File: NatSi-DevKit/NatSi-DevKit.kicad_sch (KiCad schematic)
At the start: 47 parts, among them J1 USB_TypeC, J2 Conn_01x22_Pin, J3 Conn_01x22_Pin, J4 MEM2067-02-180-00-A_REVB, SW1 SW_Push, SW2 SW_Push, SW3 SW_Push, U1 USBLC6-2SC6, U2 ESP32-S3-WROOM-1, U3 NCP1117-3.3_SOT223

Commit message: PCB update - traces
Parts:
- J1: footprint sumec_brd:USB_Type_C -> sumec_brd:HRO_TYPE-C-31-M-12
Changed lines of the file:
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@@
 			)
 		)
-		(property "Footprint" "sumec_brd:USB_Type_C"
+		(property "Footprint" "sumec_brd:HRO_TYPE-C-31-M-12"
 			(at 133.35 167.64 0)
 			(effects

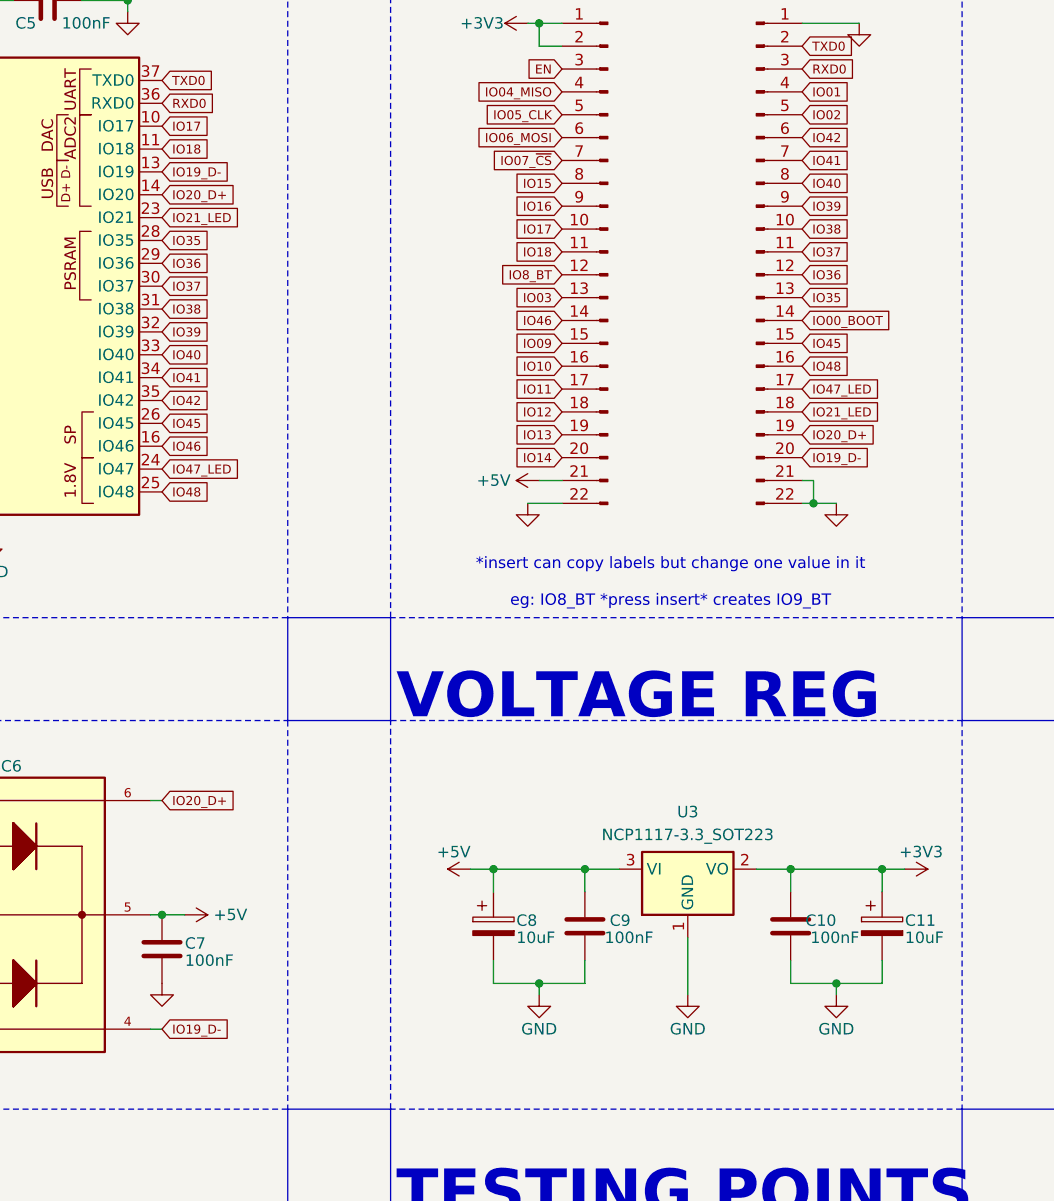
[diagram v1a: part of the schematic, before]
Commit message: Board update silkscreen and rouitign
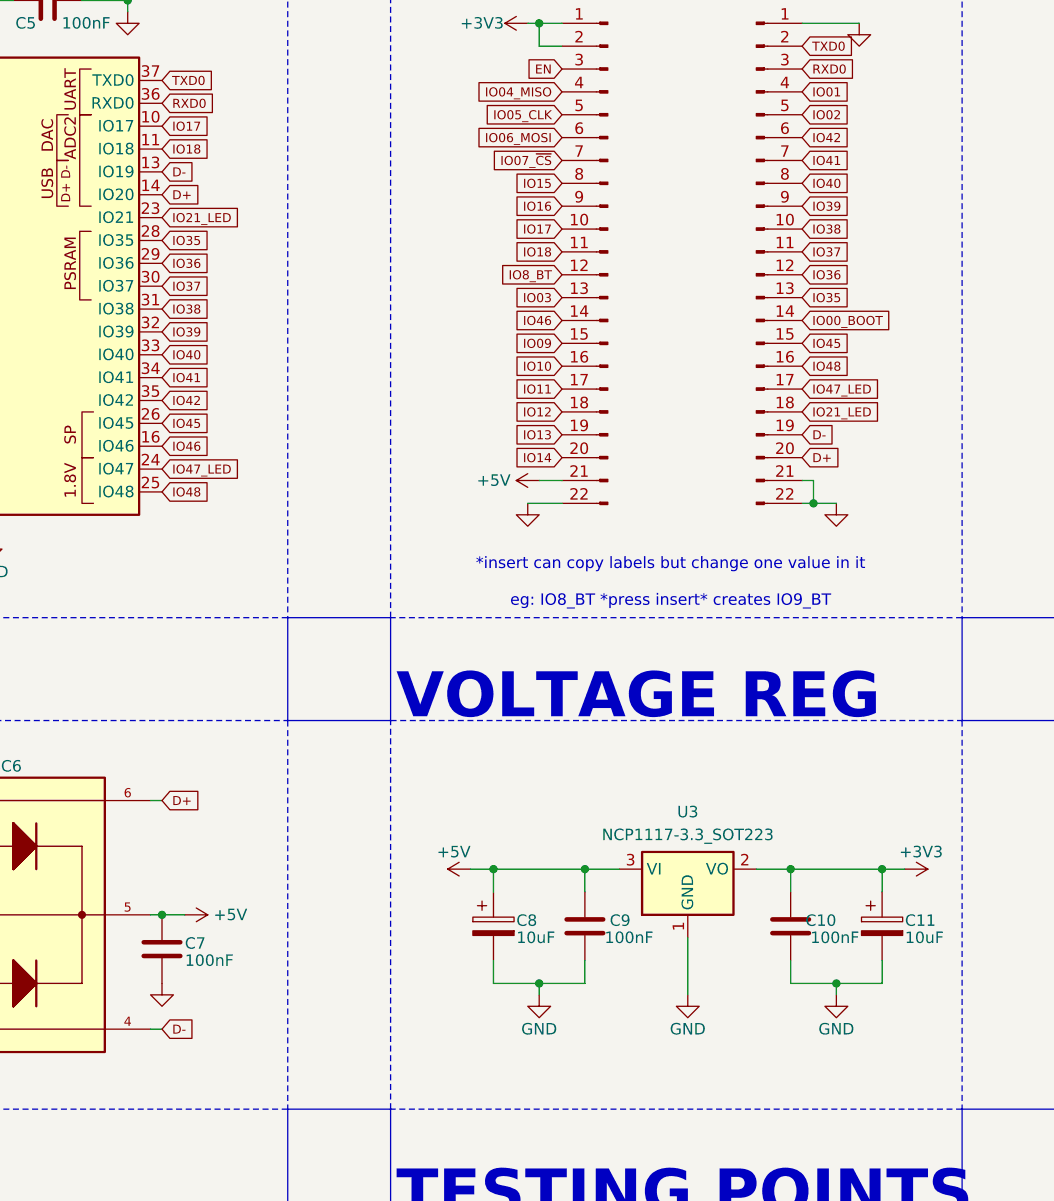
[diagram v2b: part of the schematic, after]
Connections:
- net IO19_D- renamed D-
- net D-: now also J3.19 (Pin_19); no longer J3.20 (Pin_20)
- net IO20_D+ renamed D+
- net D+: now also J3.20 (Pin_20); no longer J3.19 (Pin_19)

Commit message: Booard update
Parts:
- removed TP3: TestPoint, TestPoint:TestPoint_THTPad_D1.5mm_Drill0.7mm, symbol Connector:TestPoint
- SW1, SW2: footprint sumec_brd:SW_SPST_EVQPE1 -> Button_Switch_SMD:SW_SPST_B3U-1000P
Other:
- moved on the sheet: TP1, TP2
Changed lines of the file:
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@@
 	(wire
 		(pts
-			(xy 256.54 226.06) (xy 256.54 222.25)
+			(xy 265.43 224.79) (xy 265.43 220.98)
 		)
 		(stroke
@@
 	(wire
 		(pts
-			(xy 243.84 226.06) (xy 243.84 222.25)
+			(xy 252.73 224.79) (xy 252.73 220.98)
 		)
 		(stroke
@@
 	(wire
 		(pts
-			(xy 269.24 226.06) (xy 269.24 222.25)
-		)
-		(stroke
-			(width 0)
-			(type default)
-		)
-	)
-	(wire
-		(pts
 			(xy 247.65 67.31) (xy 247.65 69.85)
 		)
@@
 	(text "BOOT"
 		(exclude_from_sim no)
-		(at 143.51 214.63 0)
+		(at 146.05 213.995 0)
 		(effects
 			(font
@@
 				(color 0 0 0 1)
 			)
-			(justify left bottom)
 		)
 	)
@@
 	(text "ENABLE\nRESET"
 		(exclude_from_sim no)
-		(at 120.015 214.63 0)
+		(at 123.19 212.725 0)
 		(effects
 			(font
@@
 				(color 0 0 0 1)
 			)
-			(justify left bottom)
 		)
 	)
@@
 	(symbol
 		(lib_id "Connector:TestPoint")
-		(at 256.54 222.25 0)
+		(at 265.43 220.98 0)
 		(unit 1)
 		(exclude_from_sim no)
@@
 		(dnp no)
 		(property "Reference" "TP2"
-			(at 258.318 217.678 0)
+			(at 267.208 216.408 0)
 			(effects
 				(font
@@
 		)
 		(property "Value" "TestPoint"
-			(at 258.318 220.218 0)
+			(at 267.208 218.948 0)
 			(effects
 				(font
@@
 		)
 		(property "Footprint" "TestPoint:TestPoint_THTPad_D1.5mm_Drill0.7mm"
-			(at 261.62 222.25 0)
+			(at 270.51 220.98 0)
 			(effects
 				(font
@@
 		)
 		(property "Datasheet" "~"
-			(at 261.62 222.25 0)
+			(at 270.51 220.98 0)
 			(effects
 				(font
@@
 		)
 		(property "Description" "test point"
-			(at 256.54 222.25 0)
+			(at 265.43 220.98 0)
 			(effects
 				(font
@@
 	(symbol
 		(lib_id "power:+5V")
-		(at 256.54 226.06 180)
+		(at 265.43 224.79 180)
 		(unit 1)
 		(exclude_from_sim no)
@@
 		(dnp no)
 		(property "Reference" "#PWR019"
-			(at 256.54 222.25 0)
+			(at 265.43 220.98 0)
 			(effects
 				(font
@@
 		)
 		(property "Value" "+5V"
-			(at 255.27 227.965 0)
+			(at 264.16 226.695 0)
 			(effects
 				(font
@@
 		)
 		(property "Footprint" ""
-			(at 256.54 226.06 0)
+			(at 265.43 224.79 0)
 			(effects
 				(font
@@
 		)
 		(property "Datasheet" ""
-			(at 256.54 226.06 0)
+			(at 265.43 224.79 0)
 			(effects
 				(font
@@
 		)
 		(property "Description" "Power symbol creates a global label with name \"+5V\""
-			(at 256.54 226.06 0)
+			(at 265.43 224.79 0)
 			(effects
 				(font
@@
 			)
 		)
-		(property "Footprint" "sumec_brd:SW_SPST_EVQPE1"
+		(property "Footprint" "Button_Switch_SMD:SW_SPST_B3U-1000P"
 			(at 146.05 215.9 0)
 			(effects
@@
 	(symbol
 		(lib_id "Connector:TestPoint")
-		(at 243.84 222.25 0)
+		(at 252.73 220.98 0)
 		(unit 1)
 		(exclude_from_sim no)
@@
 		(dnp no)
 		(property "Reference" "TP1"
-			(at 245.618 217.678 0)
+			(at 254.508 216.408 0)
 			(effects
 				(font
@@
 		)
 		(property "Value" "TestPoint"
-			(at 245.618 220.218 0)
+			(at 254.508 218.948 0)
 			(effects
 				(font
@@
 		)
 		(property "Footprint" "TestPoint:TestPoint_THTPad_D1.5mm_Drill0.7mm"
-			(at 248.92 222.25 0)
+			(at 257.81 220.98 0)
 			(effects
 				(font
@@
 		)
 		(property "Datasheet" "~"
-			(at 248.92 222.25 0)
+			(at 257.81 220.98 0)
 			(effects
 				(font
@@
 		)
 		(property "Description" "test point"
-			(at 243.84 222.25 0)
+			(at 252.73 220.98 0)
 			(effects
 				(font
@@
 	(symbol
 		(lib_id "power:+3V3")
-		(at 243.84 226.06 180)
+		(at 252.73 224.79 180)
 		(unit 1)
 		(exclude_from_sim no)
@@
 		(dnp no)
 		(property "Reference" "#PWR017"
-			(at 243.84 222.25 0)
+			(at 252.73 220.98 0)
 			(effects
 				(font
@@
 		)
 		(property "Value" "+3V3"
-			(at 242.57 227.965 0)
+			(at 251.46 226.695 0)
 			(effects
 				(font
@@
 		)
 		(property "Footprint" ""
-			(at 243.84 226.06 0)
+			(at 252.73 224.79 0)
 			(effects
 				(font
@@
 		)
 		(property "Datasheet" ""
-			(at 243.84 226.06 0)
+			(at 252.73 224.79 0)
 			(effects
 				(font
@@
 		)
 		(property "Description" ""
-			(at 243.84 226.06 0)
+			(at 252.73 224.79 0)
 			(effects
 				(font
@@
 			)
 		)
-		(property "Footprint" "sumec_brd:SW_SPST_EVQPE1"
+		(property "Footprint" "Button_Switch_SMD:SW_SPST_B3U-1000P"
 			(at 123.19 215.9 0)
 			(effects
@@
 	)
 	(symbol
-		(lib_id "power:GND")
-		(at 269.24 226.06 0)
-		(unit 1)
-		(exclude_from_sim no)
-		(in_bom yes)
-		(on_board yes)
-		(dnp no)
-		(property "Reference" "#PWR031"
-			(at 269.24 232.41 0)
-			(effects
-				(font
-					(face "Consolas")
-					(size 1.27 1.27)
-				)
-				(hide yes)
-			)
-		)
-		(property "Value" "GND"
-			(at 269.24 229.87 0)
-			(effects
-				(font
-					(face "Consolas")
-					(size 1.27 1.27)
-				)
-			)
-		)
-		(property "Footprint" ""
-			(at 269.24 226.06 0)
-			(effects
-				(font
-					(face "Consolas")
-					(size 1.27 1.27)
-				)
-				(hide yes)
-			)
-		)
-		(property "Datasheet" ""
-			(at 269.24 226.06 0)
-			(effects
-				(font
-					(face "Consolas")
-					(size 1.27 1.27)
-				)
-				(hide yes)
-			)
-		)
-		(property "Description" "Power symbol creates a global label with name \"GND\" , ground"
-			(at 269.24 226.06 0)
-			(effects
-				(font
-					(face "Consolas")
-					(size 1.27 1.27)
-				)
-				(hide yes)
-			)
-		)
-		(pin "1"
-		)
-		(instances
-			(project "NatSi-DevKit"
-				(path "/900bd7ac-cdf9-4a2f-8b1f-2c21e3760046"
-					(reference "#PWR031")
-					(unit 1)
-				)
-			)
-		)
-	)
-	(symbol
 		(lib_id "Connector:TestPoint")
 		(at 332.74 219.71 0)
@@
 					(unit 1)
 				)
-			)
-		)
-	)
-	(symbol
-		(lib_id "Connector:TestPoint")
-		(at 269.24 222.25 0)
-		(unit 1)
-		(exclude_from_sim no)
-		(in_bom yes)
-		(on_board yes)
-		(dnp no)
-		(property "Reference" "TP3"
-			(at 271.018 217.678 0)
-			(effects
-				(font
-					(face "Consolas")
-					(size 1.27 1.27)
-				)
-				(justify left)
-			)
-		)
-		(property "Value" "TestPoint"
-			(at 271.018 220.218 0)
-			(effects
-				(font
-					(face "Consolas")
-					(size 1.27 1.27)
-				)
-				(justify left)
-			)
-		)
-		(property "Footprint" "TestPoint:TestPoint_THTPad_D1.5mm_Drill0.7mm"
-			(at 274.32 222.25 0)
-			(effects
-				(font
-					(face "Consolas")
-					(size 1.27 1.27)
-				)
-				(hide yes)
-			)
-		)
-		(property "Datasheet" "~"
-			(at 274.32 222.25 0)
-			(effects
-				(font
-					(face "Consolas")
-					(size 1.27 1.27)
-				)
-				(hide yes)
-			)
-		)
-		(property "Description" "test point"
-			(at 269.24 222.25 0)
-			(effects
-				(font
-					(face "Consolas")
-					(size 1.27 1.27)
-				)
-				(hide yes)
-			)
-		)
-		(pin "1"
-		)
-		(instances
-			(project "NatSi-DevKit"
-				(path "/900bd7ac-cdf9-4a2f-8b1f-2c21e3760046"
-					(reference "TP3")
-					(unit 1)
-				)

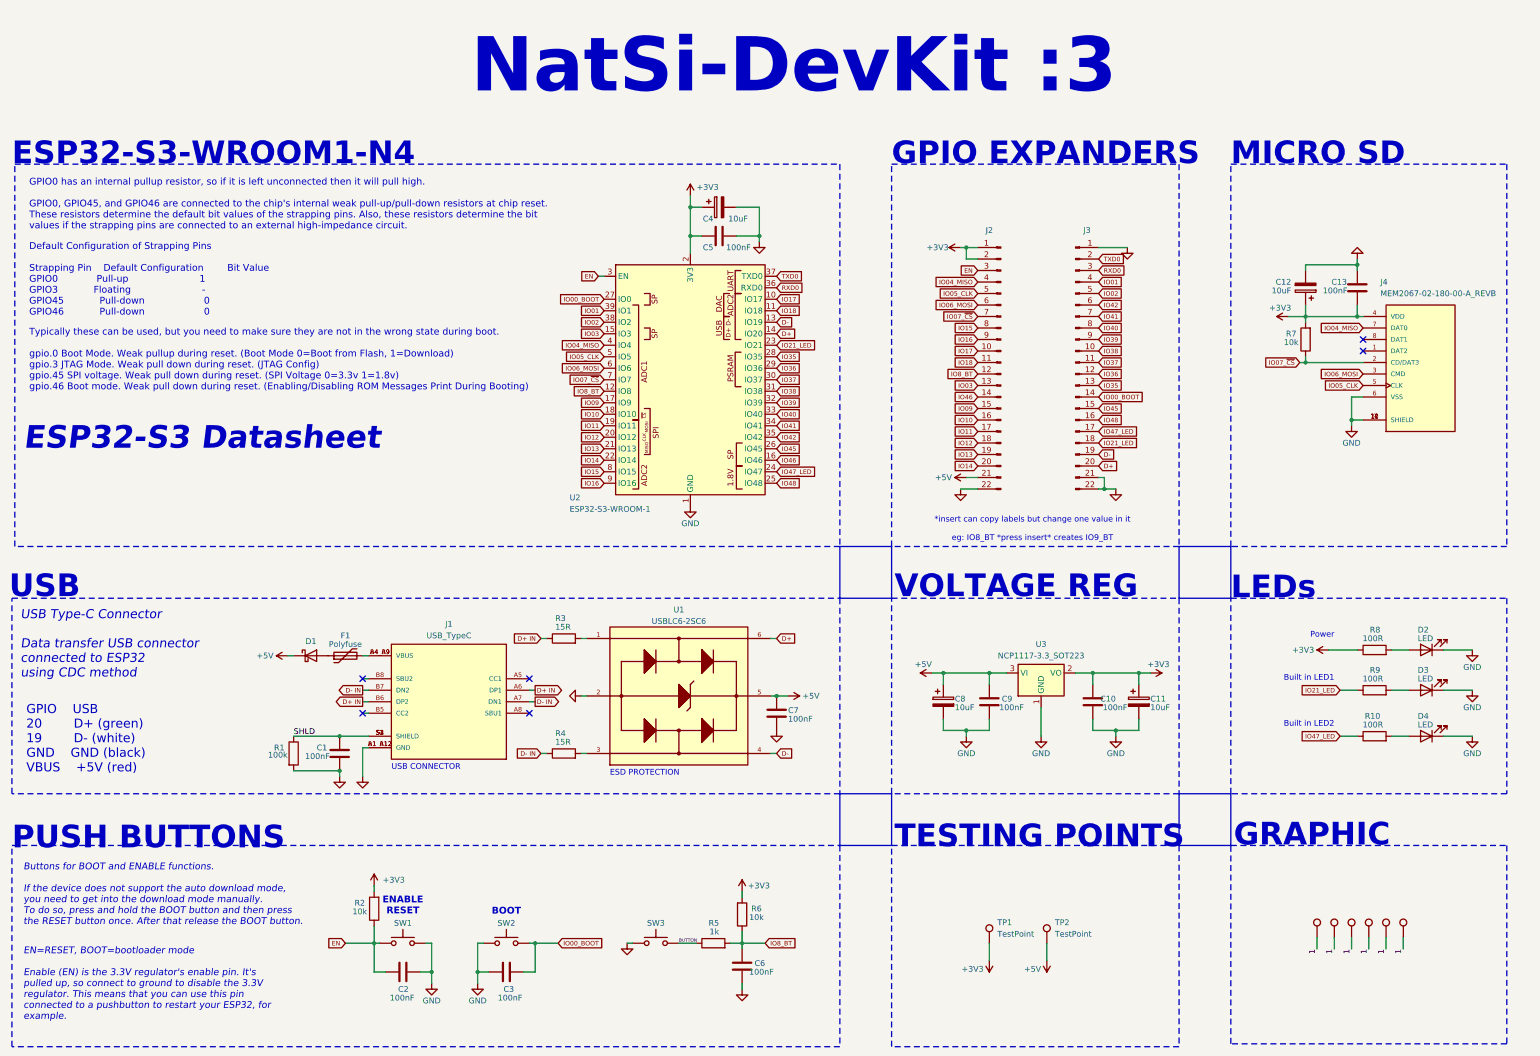
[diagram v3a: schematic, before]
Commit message: new silk, rounded tracks and soldermask
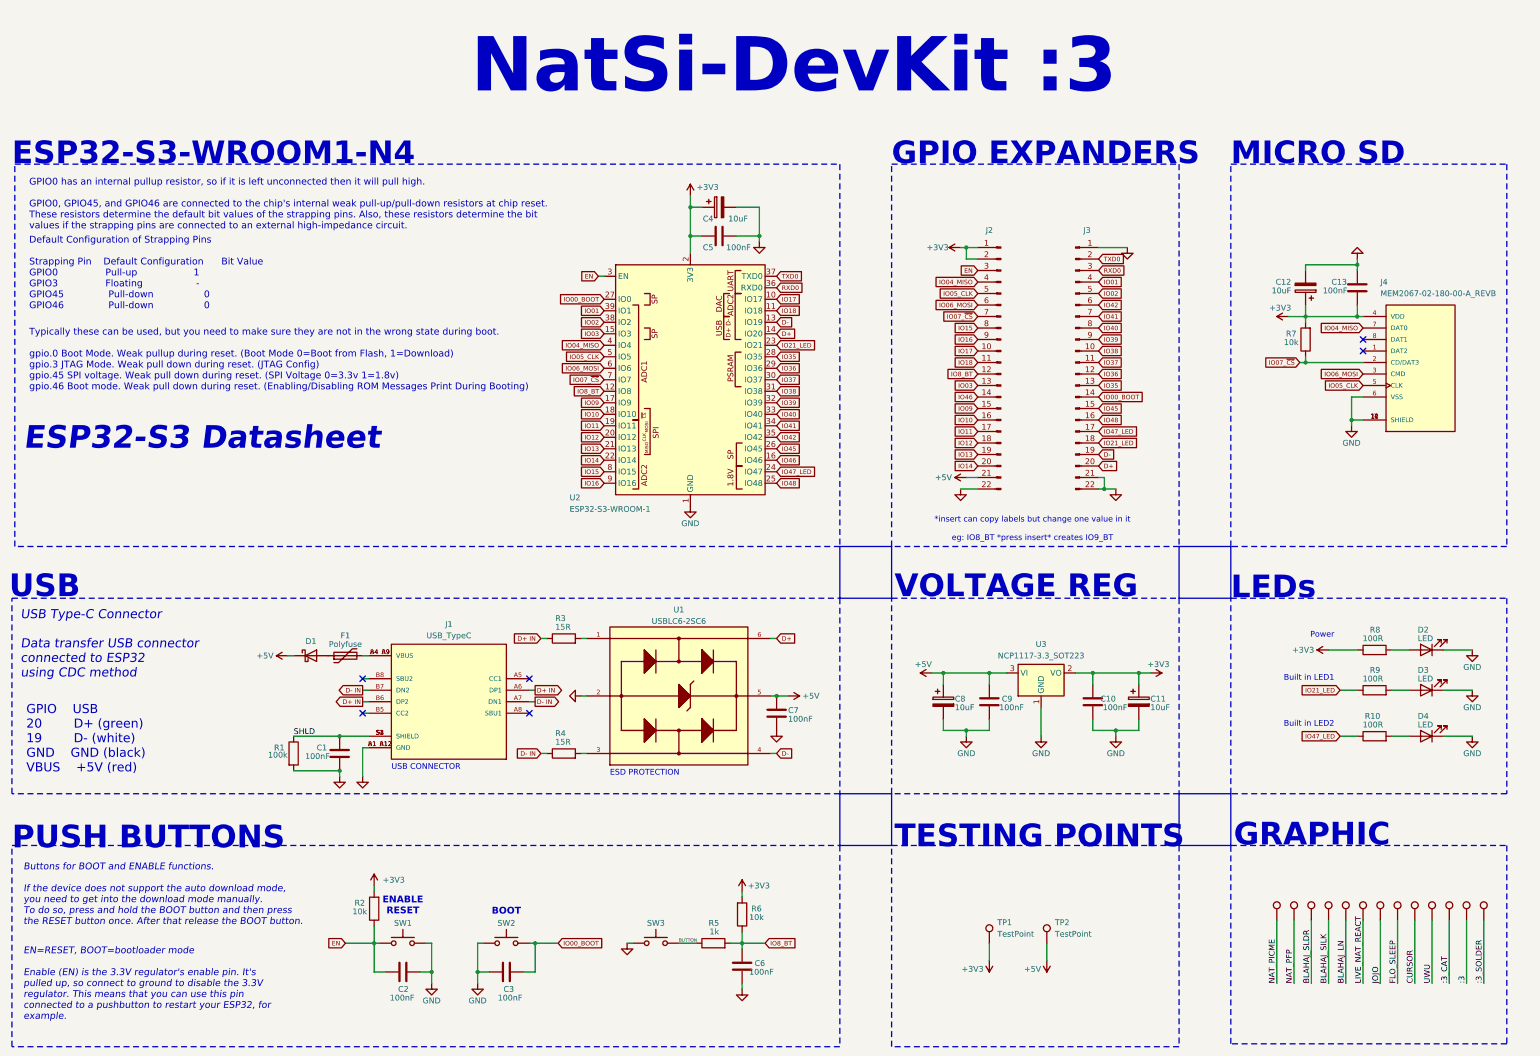
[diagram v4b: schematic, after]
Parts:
- added TP12: TestPoint, sumec_graphic:UWU_IMG, symbol Connector:TestPoint
- added TP14: TestPoint, sumec_graphic:COLON_3_IMG, symbol Connector:TestPoint
- added TP15: TestPoint, sumec_graphic:COLON_3_SOLDER, symbol Connector:TestPoint
- added TP5: TestPoint, sumec_graphic:BLAHAJ_IMG, symbol Connector:TestPoint
- added TP7: TestPoint, sumec_graphic:BLAHAJ_LINE_IMG, symbol Connector:TestPoint
- added TP8: TestPoint, sumec_graphic:LIVE_NAT_REACTION_NEG, symbol Connector:TestPoint
- added TP9: TestPoint, sumec_graphic:JOJO_SYMBOL_IMG, symbol Connector:TestPoint
- SW3: footprint sumec_brd:SW_SPST_EVQPE1 -> Button_Switch_SMD:SW_SPST_B3U-1000P
- TP10: renamed from TP7; footprint sumec_graphic:LIVE_NAT_REACTION_NEG -> sumec_graphic:FLO_SLEEP_IMG
- TP11: renamed from TP9; footprint sumec_graphic:FLO_POINTING_IMG -> sumec_graphic:CURSOR_IMG
- TP13: renamed from TP8; footprint sumec_graphic:FLO_SLEEP_IMG -> sumec_graphic:COLON_3_CAT_IMG
- TP6: footprint sumec_graphic:FLO_FRONT_C_IMG -> sumec_graphic:BLAHAJ_IMG_silk
- renumbered TP4 to TP3, TP5 to TP4
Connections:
- removed net 1: TP10.1, TP11.1, TP13.1, TP3.1, TP4.1, TP6.1
- new net:3: TP14.1
- new net:3_CAT: TP13.1
- new net:3_SOLDER: TP15.1
- new net BLAHAJ_LN: TP7.1
- new net BLAHAJ_SILK: TP6.1
- new net BLAHAJ_SLDR: TP5.1
- new net CURSOR: TP11.1
- new net FLO_SLEEP: TP10.1
- new net JOJO: TP9.1
- new net LIVE_NAT_REACT: TP8.1
- new net NAT_PFP: TP4.1
- new net NAT_PICME: TP3.1
- new net UWU: TP12.1

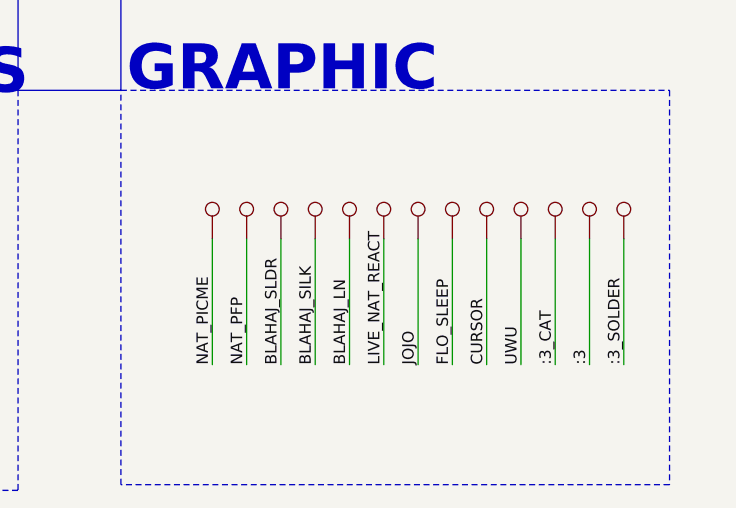
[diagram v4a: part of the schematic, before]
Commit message: PCB update silkscreen
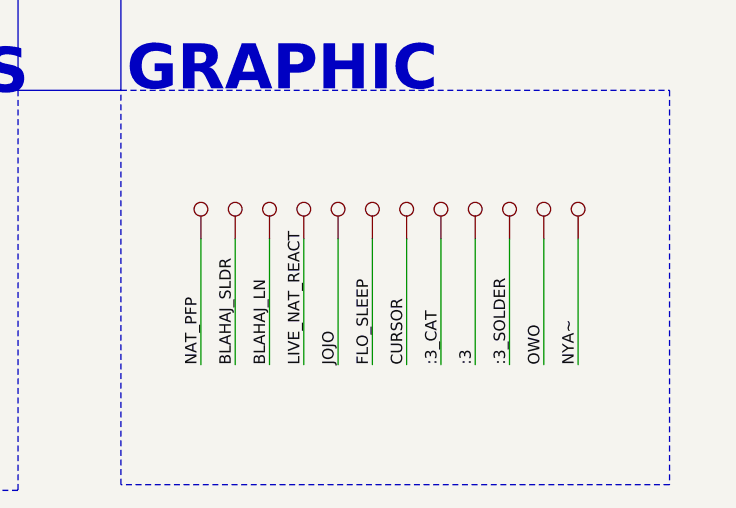
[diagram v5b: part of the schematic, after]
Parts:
- removed TP12: TestPoint, sumec_graphic:UWU_IMG, symbol Connector:TestPoint
- removed TP3: TestPoint, sumec_graphic:NATI_PICME_IMG, symbol Connector:TestPoint
- removed TP6: TestPoint, sumec_graphic:BLAHAJ_IMG_silk, symbol Connector:TestPoint
- added TP15: TestPoint, sumec_graphic:OWO_IMG, symbol Connector:TestPoint
- added TP16: TestPoint, sumec_graphic:NYA_IMG, symbol Connector:TestPoint
- renumbered TP13 to TP12, TP14 to TP13, TP15 to TP14
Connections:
- new net NYA~: TP16.1
- new net OWO: TP15.1
